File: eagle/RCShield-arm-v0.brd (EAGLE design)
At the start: 92.7 x 82.5 mm, 48 parts, among them U3 TS5A3157DBV, U4 XBEE, U5 TS5A3157DBV, X1 USB

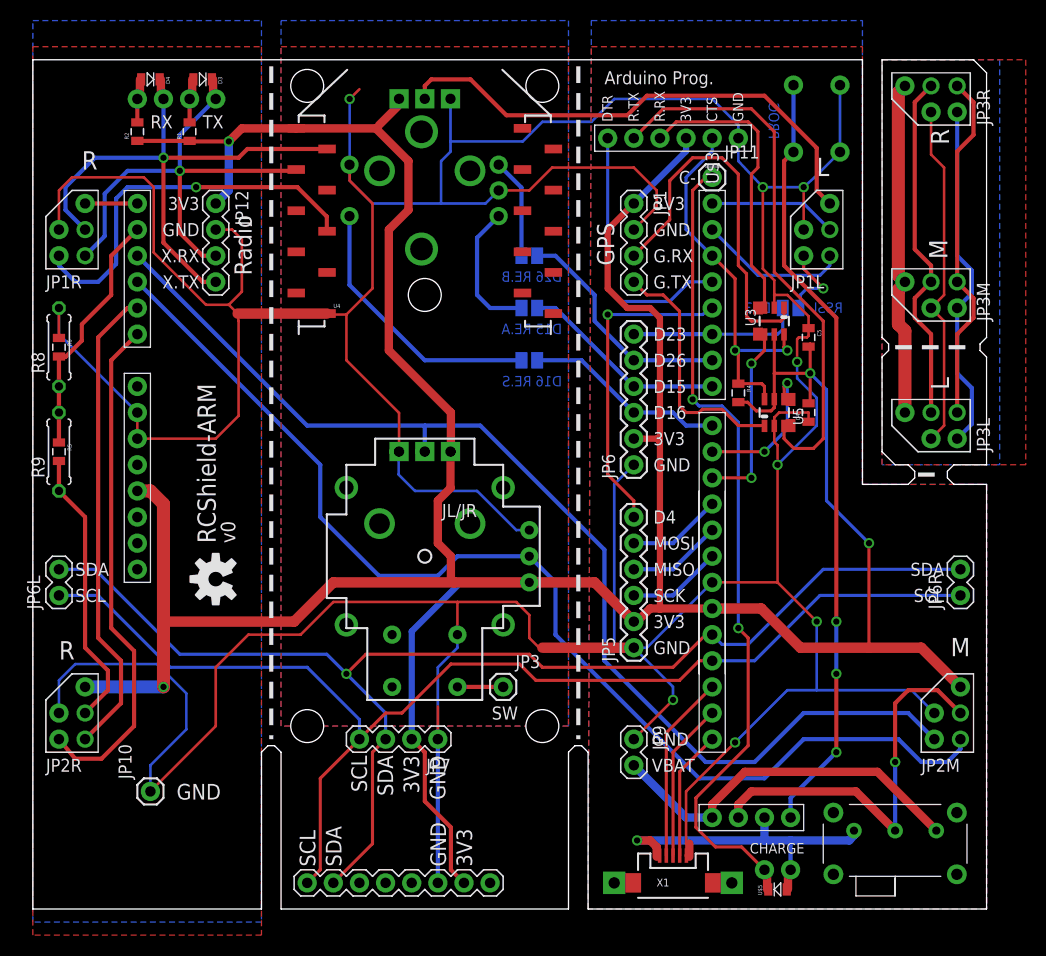
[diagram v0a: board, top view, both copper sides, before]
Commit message: 
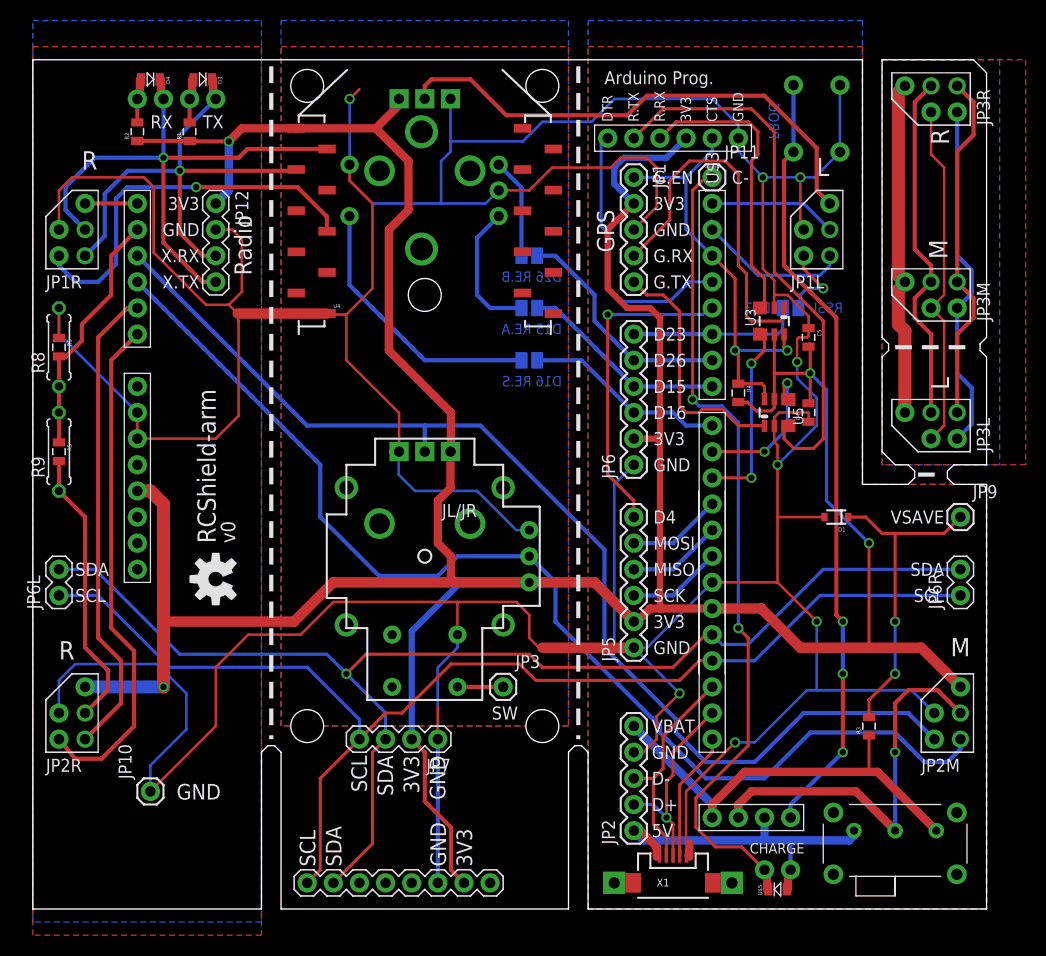
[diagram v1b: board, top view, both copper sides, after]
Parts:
- added D1: 2V4, SparkFun:SOD-323
- added JP2: (no value), SparkFun:1X05
- added R3: 100k, SparkFun:0805
- JP1: value GPS -> (none); device wibauxl:1X04 -> SparkFun:1X05
- JP9: value BAT -> (none); device wibauxl:1X02 -> SparkFun:1X01
- moved JP9 38.4 mm to (90.2, 38.1), turned to 0 degrees
- moved JP1 2.54 mm to (58.4, 71.1)
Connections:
- net N$9 renamed ID
- removed net N$2: U$3.USB_D-, X1.D-
- removed net N$3: U$3.USB_D+, X1.D+
- new net D+: JP2.2, U$3.USB_D+, X1.D+
- new net D-: JP2.3, U$3.USB_D-, X1.D-
- new net VSAVE: D1.1, JP9.1, R3.2
- net 3.3V: now also JP1.2; no longer JP1.1
- net D22: now also JP1.1
- net GND: now also D1.2, JP1.3, JP2.4; no longer JP1.2, JP9.1
- net GPS_RX: now also JP1.4; no longer JP1.3
- net GPS_TX: now also JP1.5; no longer JP1.4
- net VBAT: now also JP2.5, R3.1; no longer JP9.2
- net VUSB: now also JP2.1
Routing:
- net VSAVE: track 0.00 -> 31.4 mm, vias 0 -> 2
- net D-: track 0.00 -> 21.2 mm
- net D+: track 0.00 -> 19.7 mm, vias 0 -> 1
- net N$2: track 18.2 -> 0.00 mm
- net N$3: track 15.4 -> 0.00 mm
- net GND: track 530.5 -> 539.3 mm
- net VBAT: track 36.5 -> 42.8 mm
- net D22: track 37.7 -> 42.8 mm
- net 3.3V: track 341.6 -> 345.6 mm
- net VUSB: track 30.3 -> 31.7 mm, vias 1 -> 0
- net D3: track 26.1 -> 26.6 mm
- net N$1: track 75.6 -> 76.1 mm
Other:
- board text added: "5V"
- board text added: "D+"
- board text added: "D-"
- board text added: "G.EN"
- board text added: "RCShield-arm"
- board text added: "VSAVE"
- board text removed: "RCShield-ARM"
